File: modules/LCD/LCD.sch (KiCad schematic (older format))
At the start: 13 parts, among them J1 Conn_01x10_Male, J2 Conn_01x10_Male, J3 Conn_01x04_Female, J4 Conn_01x02_Female, U1 74LS139

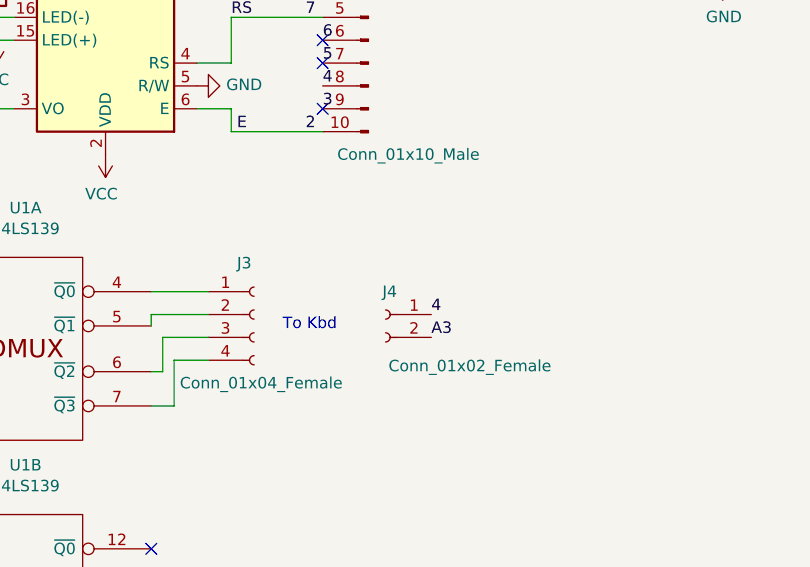
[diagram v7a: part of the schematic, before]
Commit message: Wrong PCB orientation! Swap pinheader :( Smaller holes for LCD. Add pull-ups, add pin names.
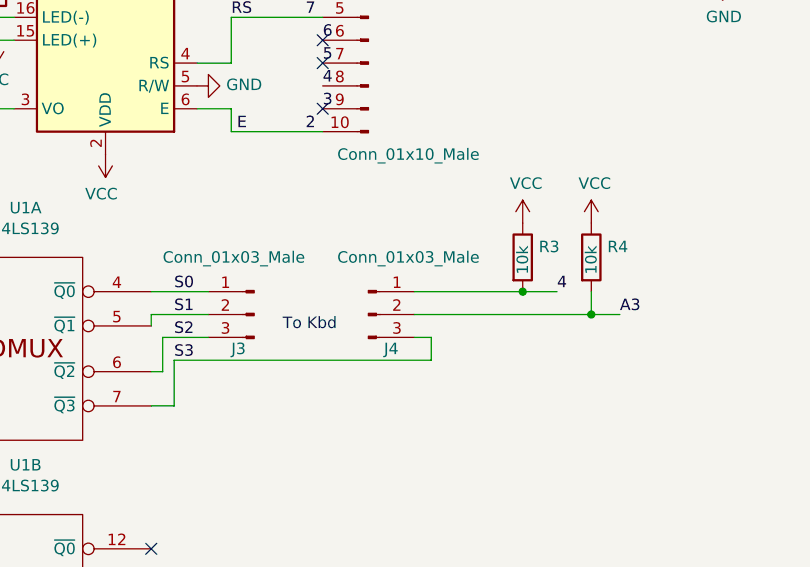
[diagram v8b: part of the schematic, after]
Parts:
- removed J3: Conn_01x04_Female, Connector_PinSocket_2.54mm:PinSocket_1x04_P2.54mm_Vertical, symbol Connector:Conn_01x04_Female
- removed J4: Conn_01x02_Female, Connector_PinSocket_2.54mm:PinSocket_1x02_P2.54mm_Vertical, symbol Connector:Conn_01x02_Female
- added J3, J4: Conn_01x03_Male, Connector_PinHeader_2.54mm:PinHeader_1x03_P2.54mm_Horizontal, symbol Connector:Conn_01x03_Male
- added R3, R4: 10k, Resistor_SMD:R_0805_2012Metric_Pad1.20x1.40mm_HandSolder, symbol Device:R
- R1, R2: footprint Resistor_SMD:R_0805_2012Metric_Pad1.15x1.40mm_HandSolder -> Resistor_SMD:R_0805_2012Metric_Pad1.20x1.40mm_HandSolder
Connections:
- net 4: now also J4.1 (Pin_1), R3.2
- net A3: now also J4.2 (Pin_2), R4.2
- net VCC: now also R3.1, R4.1
- net S0: now reaches U1.4 (~Q0)
- net S0: now also J3.1 (Pin_1)
- net S1: now reaches U1.5 (~Q1)
- net S1: now also J3.2 (Pin_2)
- net S2: now reaches U1.6 (~Q2)
- net S2: now also J3.3 (Pin_3)
- net S3: now reaches U1.7 (~Q3)
- net S3: now also J4.3 (Pin_3)
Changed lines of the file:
@@
 F 0 "R1" H 2256 2204 50  0000 R CNN
 F 1 "20" H 2256 2295 50  0000 R CNN
-F 2 "Resistor_SMD:R_0805_2012Metric_Pad1.15x1.40mm_HandSolder" V 2255 2250 50  0001 C CNN
+F 2 "Resistor_SMD:R_0805_2012Metric_Pad1.20x1.40mm_HandSolder" V 2255 2250 50  0001 C CNN
 F 3 "~" H 2325 2250 50  0001 C CNN
 	1    2325 2250
@@
 F 0 "R2" V 1675 4725 50  0000 C CNN
 F 1 "10k" V 1750 4725 50  0000 C CNN
-F 2 "Resistor_SMD:R_0805_2012Metric_Pad1.15x1.40mm_HandSolder" V 1680 4725 50  0001 C CNN
+F 2 "Resistor_SMD:R_0805_2012Metric_Pad1.20x1.40mm_HandSolder" V 1680 4725 50  0001 C CNN
 F 3 "~" H 1750 4725 50  0001 C CNN
 	1    1750 4725
@@
 NoConn ~ 3000 5075
 NoConn ~ 3000 5225
-$Comp
-L Connector:Conn_01x04_Female J3
-U 1 1 5FC38C89
-P 3450 3700
-F 0 "J3" H 3375 3925 50  0000 L CNN
-F 1 "Conn_01x04_Female" H 3125 3400 50  0000 L CNN
-F 2 "Connector_PinSocket_2.54mm:PinSocket_1x04_P2.54mm_Vertical" H 3450 3700 50  0001 C CNN
-F 3 "~" H 3450 3700 50  0001 C CNN
-	1    3450 3700
-	1    0    0    -1
-$EndComp
 Wire Wire Line
 	3000 3600 3250 3600
@@
 Wire Wire Line
 	3100 4100 3100 3900
-Wire Wire Line
-	3100 3900 3250 3900
 Text Notes 3575 3775 0    50   ~ 0
 To Kbd
+Text Label 4775 3600 0    50   ~ 0
+4
+Text Label 5050 3700 0    50   ~ 0
+A3
 $Comp
-L Connector:Conn_01x02_Female J4
-U 1 1 5FC3BBE8
-P 4025 3700
-F 0 "J4" H 3975 3800 50  0000 L CNN
-F 1 "Conn_01x02_Female" H 3300 3475 50  0000 L CNN
-F 2 "Connector_PinSocket_2.54mm:PinSocket_1x02_P2.54mm_Vertical" H 4025 3700 50  0001 C CNN
-F 3 "~" H 4025 3700 50  0001 C CNN
-	1    4025 3700
+L Connector:Conn_01x03_Male J3
+U 1 1 602F21F3
+P 3450 3700
+F 0 "J3" H 3550 3550 50  0000 R CNN
+F 1 "Conn_01x03_Male" H 3850 3950 50  0000 R CNN
+F 2 "Connector_PinHeader_2.54mm:PinHeader_1x03_P2.54mm_Horizontal" H 3450 3700 50  0001 C CNN
+F 3 "~" H 3450 3700 50  0001 C CNN
+	1    3450 3700
 	-1   0    0    -1
 $EndComp
-Text Label 4225 3700 0    50   ~ 0
-4
-Text Label 4225 3800 0    50   ~ 0
-A3
+$Comp
+L Connector:Conn_01x03_Male J4
+U 1 1 602F2840
+P 3950 3700
+F 0 "J4" H 4050 3550 50  0000 C CNN
+F 1 "Conn_01x03_Male" H 4125 3950 50  0000 C CNN
+F 2 "Connector_PinHeader_2.54mm:PinHeader_1x03_P2.54mm_Horizontal" H 3950 3700 50  0001 C CNN
+F 3 "~" H 3950 3700 50  0001 C CNN
+	1    3950 3700
+	1    0    0    -1
+$EndComp
+Wire Wire Line
+	4225 3900 4225 3800
+Wire Wire Line
+	4225 3800 4150 3800
+Wire Wire Line
+	3100 3900 4225 3900
+Text Label 3100 3600 0    50   ~ 0
+S0
+Text Label 3100 3700 0    50   ~ 0
+S1
+Text Label 3100 3800 0    50   ~ 0
+S2
+Text Label 3100 3900 0    50   ~ 0
+S3
+$Comp
+L Device:R R3
+U 1 1 6031DA83
+P 4625 3450
+F 0 "R3" H 4695 3496 50  0000 L CNN
+F 1 "10k" V 4625 3375 50  0000 L CNN
+F 2 "Resistor_SMD:R_0805_2012Metric_Pad1.20x1.40mm_HandSolder" V 4555 3450 50  0001 C CNN
+F 3 "~" H 4625 3450 50  0001 C CNN
+	1    4625 3450
+	1    0    0    -1
+$EndComp
+$Comp
+L Device:R R4
+U 1 1 6031E135
+P 4925 3450
+F 0 "R4" H 4995 3496 50  0000 L CNN
+F 1 "10k" V 4925 3375 50  0000 L CNN
+F 2 "Resistor_SMD:R_0805_2012Metric_Pad1.20x1.40mm_HandSolder" V 4855 3450 50  0001 C CNN
+F 3 "~" H 4925 3450 50  0001 C CNN
+	1    4925 3450
+	1    0    0    -1
+$EndComp
+Wire Wire Line
+	4150 3600 4625 3600
+Connection ~ 4625 3600
+Wire Wire Line
+	4625 3600 4775 3600
+Wire Wire Line
+	4150 3700 4925 3700
+Wire Wire Line
+	4925 3600 4925 3700
+Connection ~ 4925 3700
+Wire Wire Line
+	4925 3700 5050 3700
+$Comp
+L power:VCC #PWR03
+U 1 1 603214A3
+P 4625 3300
+F 0 "#PWR03" H 4625 3150 50  0001 C CNN
+F 1 "VCC" H 4640 3473 50  0000 C CNN
+F 2 "" H 4625 3300 50  0001 C CNN
+F 3 "" H 4625 3300 50  0001 C CNN
+	1    4625 3300
+	1    0    0    -1
+$EndComp
+$Comp
+L power:VCC #PWR04
+U 1 1 60321F80
+P 4925 3300
+F 0 "#PWR04" H 4925 3150 50  0001 C CNN
+F 1 "VCC" H 4940 3473 50  0000 C CNN
+F 2 "" H 4925 3300 50  0001 C CNN
+F 3 "" H 4925 3300 50  0001 C CNN
+	1    4925 3300
+	1    0    0    -1
+$EndComp
 $EndSCHEMATC
